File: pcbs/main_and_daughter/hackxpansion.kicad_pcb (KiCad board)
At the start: 4 copper layers, 52 x 69 mm, 97 parts, among them CN1 533981471, CN2 533981471, CN3 533981471, CN4 533981471, IC1 ADS7128IRTET, J1 Conn_01x03_MountingPin, J2 USB_C_Receptacle_USB2.0_14P, Q1 BSS138, Q2 2N7002, SW1 SW_Push, SW2 SW_Push, SW3 SW_On_Off, U2 RP2354B, U5 SPX3819M5-L-3-3, U7 BQ24075RGT, U8 USBLC6-2SC6, Y1 ABM8-272-T3

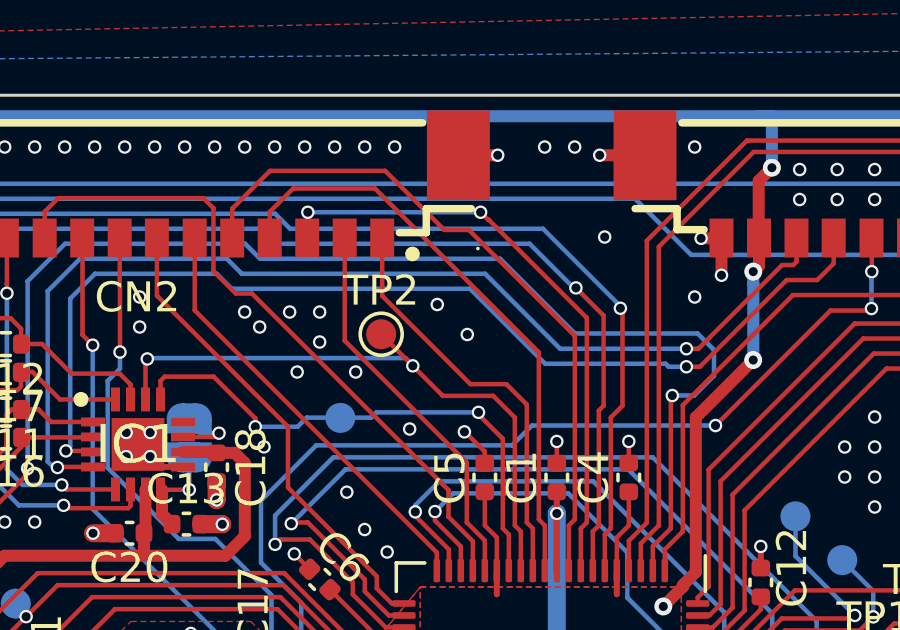
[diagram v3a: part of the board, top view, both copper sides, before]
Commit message: switcheed bank 0 pin 5 and 6 cuz i messed up
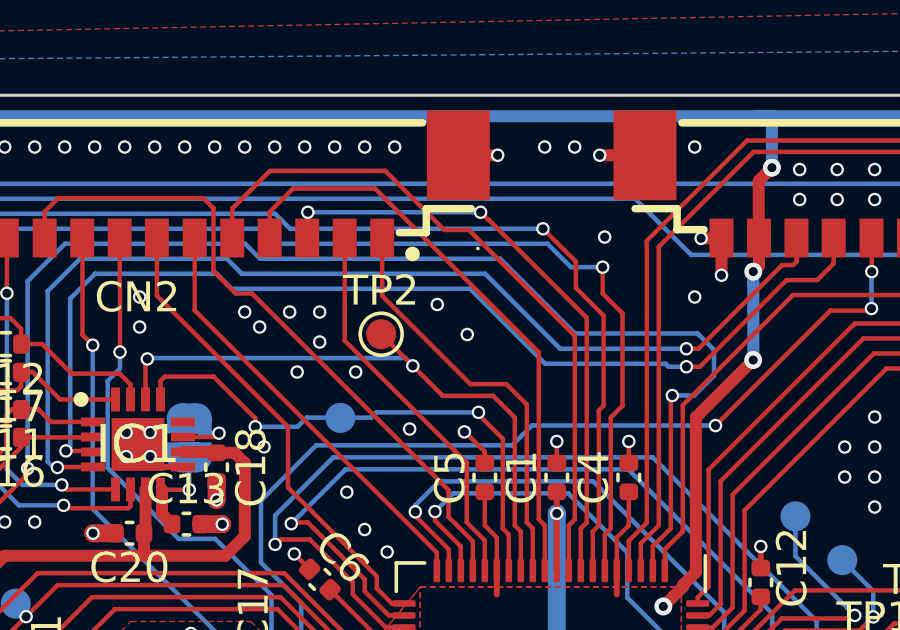
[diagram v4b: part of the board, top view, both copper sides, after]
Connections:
- U2 pad 6: /Main Board/Module Bay 0/GPIO6 -> /Main Board/Module Bay 0/GPIO5
- U2 pad 7: /Main Board/Module Bay 0/GPIO5 -> /Main Board/Module Bay 0/GPIO6
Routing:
- net /Main Board/Module Bay 0/GPIO5: track 69.6 -> 70.9 mm
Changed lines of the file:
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@@
 		)
 		(embedded_fonts no)
-		(model "${KICAD6_3DMODEL_DIR}/Capacitor_SMD.3dshapes/C_0402_1005Metric.wrl"
+		(model "${KICAD10_3DMODEL_DIR}/Capacitor_SMD.3dshapes/C_0402_1005Metric.step"
 			(offset
 				(xyz 0 0 0)
@@
 		)
 		(embedded_fonts no)
-		(model "${KICAD6_3DMODEL_DIR}/Capacitor_SMD.3dshapes/C_0402_1005Metric.wrl"
+		(model "${KICAD10_3DMODEL_DIR}/Capacitor_SMD.3dshapes/C_0402_1005Metric.step"
 			(offset
 				(xyz 0 0 0)
@@
 			(unit
 				(name "A")
-				(pins "15" "4" "14" "6" "5" "12" "16" "13" "8" "17" "10" "11" "2" "3"
+				(pins "15" "4" "14" "6" "5" "12" "16" "13" "17" "8" "10" "11" "2" "3"
 					"1" "7" "9"
 				)
@@
 			(layers "F.Cu" "F.Mask" "F.Paste")
 			(roundrect_rratio 0.25)
-			(net "/Main Board/Module Bay 0/GPIO6")
+			(net "/Main Board/Module Bay 0/GPIO5")
 			(pinfunction "GPIO8_6")
 			(pintype "bidirectional")
@@
 			(layers "F.Cu" "F.Mask" "F.Paste")
 			(roundrect_rratio 0.25)
-			(net "/Main Board/Module Bay 0/GPIO5")
+			(net "/Main Board/Module Bay 0/GPIO6")
 			(pinfunction "GPIO9_7")
 			(pintype "bidirectional")
@@
 	)
 	(segment
-		(start 130.16 65)
-		(end 130.23 65.07)
-		(width 0.15)
-		(layer "F.Cu")
-		(net "/Main Board/Module Bay 0/GPIO6")
-	)
-	(segment
 		(start 103.55 90.1)
 		(end 104.065 90.615)
@@
 	)
 	(segment
-		(start 129.640001 72.539999)
-		(end 129.640001 73.743499)
+		(start 128.678199 64.321801)
+		(end 128.678199 63.448199)
 		(width 0.15)
 		(layer "F.Cu")
@@
 	)
 	(segment
-		(start 129.840001 72.34)
-		(end 129.640001 72.539999)
+		(start 128.678199 64.321801)
+		(end 129.6 65.243602)
 		(width 0.15)
 		(layer "F.Cu")
@@
 	)
 	(segment
-		(start 129.840001 68.64)
-		(end 129.840001 72.34)
+		(start 129.240002 72.44)
+		(end 129.240002 73.743501)
 		(width 0.15)
 		(layer "F.Cu")
@@
 	)
 	(segment
-		(start 130.23 68.250001)
-		(end 129.840001 68.64)
+		(start 129.6 65.243602)
+		(end 129.6 68.25)
 		(width 0.15)
 		(layer "F.Cu")
@@
 	)
 	(segment
-		(start 130.23 65.07)
-		(end 130.23 68.250001)
+		(start 129.440002 68.409998)
+		(end 129.440002 72.239999)
+		(width 0.15)
+		(layer "F.Cu")
+		(net "/Main Board/Module Bay 0/GPIO6")
+	)
+	(segment
+		(start 128.678199 63.448199)
+		(end 127.58 62.35)
+		(width 0.15)
+		(layer "F.Cu")
+		(net "/Main Board/Module Bay 0/GPIO6")
+	)
+	(segment
+		(start 129.6 68.25)
+		(end 129.440002 68.409998)
+		(width 0.15)
+		(layer "F.Cu")
+		(net "/Main Board/Module Bay 0/GPIO6")
+	)
+	(segment
+		(start 129.440002 72.239999)
+		(end 129.240002 72.44)
 		(width 0.15)
 		(layer "F.Cu")
@@
 	)
 	(via
-		(at 130.16 65)
+		(at 103.25 90.1)
 		(size 0.45)
 		(drill 0.3)
@@
 	)
 	(via
-		(at 103.25 90.1)
+		(at 127.58 62.35)
 		(size 0.45)
 		(drill 0.3)
@@
 	)
 	(segment
-		(start 127.58 62.35)
-		(end 130.16 64.93)
-		(width 0.15)
-		(layer "B.Cu")
-		(net "/Main Board/Module Bay 0/GPIO6")
-	)
-	(segment
 		(start 106.65 83.369718)
 		(end 106.65 64.63)
@@
 	)
 	(segment
-		(start 130.16 64.93)
-		(end 130.16 65)
-		(width 0.15)
-		(layer "B.Cu")
-		(net "/Main Board/Module Bay 0/GPIO6")
-	)
-	(segment
 		(start 106.65 64.63)
 		(end 109.43 61.85)
@@
 	)
 	(segment
-		(start 103.75 90.98)
-		(end 110.979998 90.98)
+		(start 129.57 64.51)
+		(end 130.23 65.17)
 		(width 0.15)
 		(layer "F.Cu")
@@
 	)
 	(segment
-		(start 128.678199 64.321801)
-		(end 129.6 65.243602)
+		(start 129.840001 72.34)
+		(end 129.640001 72.539999)
 		(width 0.15)
 		(layer "F.Cu")
@@
 	)
 	(segment
-		(start 129.240002 72.44)
-		(end 129.240002 73.743501)
+		(start 103.75 90.98)
+		(end 110.979998 90.98)
 		(width 0.15)
 		(layer "F.Cu")
@@
 	)
 	(segment
-		(start 129.6 65.243602)
-		(end 129.6 68.25)
+		(start 129.57 63.63)
+		(end 129.57 64.51)
 		(width 0.15)
 		(layer "F.Cu")
@@
 	)
 	(segment
-		(start 129.440002 68.409998)
-		(end 129.440002 72.239999)
+		(start 129.640001 72.539999)
+		(end 129.640001 73.743499)
 		(width 0.15)
 		(layer "F.Cu")
@@
 	)
 	(segment
-		(start 110.979998 90.98)
-		(end 112.079998 92.08)
+		(start 130.23 65.17)
+		(end 130.23 68.250001)
 		(width 0.15)
 		(layer "F.Cu")
@@
 	)
 	(segment
-		(start 129.6 68.25)
-		(end 129.440002 68.409998)
+		(start 130.23 68.250001)
+		(end 129.840001 68.64)
 		(width 0.15)
 		(layer "F.Cu")
@@
 	)
 	(segment
-		(start 129.440002 72.239999)
-		(end 129.240002 72.44)
+		(start 129.840001 68.64)
+		(end 129.840001 72.34)
+		(width 0.15)
+		(layer "F.Cu")
+		(net "/Main Board/Module Bay 0/GPIO5")
+	)
+	(segment
+		(start 110.979998 90.98)
+		(end 112.079998 92.08)
 		(width 0.15)
 		(layer "F.Cu")
@@
 	)
 	(via
-		(at 128.678199 64.321801)
+		(at 103.75 90.98)
 		(size 0.45)
 		(drill 0.3)
@@
 	)
 	(via
-		(at 103.75 90.98)
+		(at 129.57 63.63)
 		(size 0.45)
 		(drill 0.3)
@@
 	)
 	(segment
-		(start 128.678199 64.321801)
-		(end 128.605735 64.321801)
+		(start 103.75 87.269718)
+		(end 103.75 90.98)
 		(width 0.15)
 		(layer "B.Cu")
@@
 	)
 	(segment
-		(start 107.15 83.869718)
-		(end 103.75 87.269718)
+		(start 127.73 62.85)
+		(end 118.65 62.85)
 		(width 0.15)
 		(layer "B.Cu")
@@
 	)
 	(segment
-		(start 107.15 64.88)
-		(end 107.15 83.869718)
+		(start 129.57 63.63)
+		(end 128.51 63.63)
 		(width 0.15)
 		(layer "B.Cu")
@@
 	)
 	(segment
-		(start 103.75 87.269718)
-		(end 103.75 90.98)
+		(start 128.51 63.63)
+		(end 127.73 62.85)
 		(width 0.15)
 		(layer "B.Cu")
@@
 	)
 	(segment
-		(start 128.605735 64.321801)
-		(end 127.133934 62.85)
+		(start 118.15 62.35)
+		(end 109.68 62.35)
 		(width 0.15)
 		(layer "B.Cu")
@@
 	)
 	(segment
-		(start 127.133934 62.85)
-		(end 118.65 62.85)
+		(start 107.15 64.88)
+		(end 107.15 83.869718)
 		(width 0.15)
 		(layer "B.Cu")
@@
 	)
 	(segment
-		(start 118.15 62.35)
-		(end 109.68 62.35)
+		(start 109.68 62.35)
+		(end 107.15 64.88)
 		(width 0.15)
 		(layer "B.Cu")
@@
 	)
 	(segment
-		(start 109.68 62.35)
-		(end 107.15 64.88)
+		(start 107.15 83.869718)
+		(end 103.75 87.269718)
 		(width 0.15)
 		(layer "B.Cu")
